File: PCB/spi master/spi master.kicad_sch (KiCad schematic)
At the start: 16 parts, among them J1 n8 Bus Connector, J2 Conn_01x09, U1 74LS08, U10 74HC273, U11 74HC245, U2 74LS393, U3 74HC04, U4 74LS139, U5 74HC595, U6 74HC165, U8 74HC74, U9 74LS153

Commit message: Worked on Spi master a little bit
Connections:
- net DIV0 is gone; now on net DEN: U10.2 (Q0), U11.2 (A0), U9.14 (S0)
- net DIV1 is gone; now on net DEN: U10.5 (Q1), U11.3 (A1), U9.2 (S1)
- net IEN is gone; now on net DEN: U1.13, U10.15 (Q5), U11.7 (A5)
- net ITC is gone; now on net DEN: U1.12, U11.9 (A7), U8.5 (Q)
- net SEL0 is gone; now on net DEN: U10.6 (Q2), U11.4 (A2), U4.2 (A0)
- net SEL1 is gone; now on net DEN: U10.9 (Q3), U11.5 (A3), U4.3 (A1)
- net UNUSED is gone; now on net DEN: U10.16 (Q6), U11.8 (A6)
- net ~{CS3} is gone; now on net ~{CS2}: J2.8 (Pin_8), U4.7 (O3)
- net CLK: now also U9.6 (I0a)
- net at U2.3 (Q0): no longer U9.6 (I0a)
- no-connect marks 20 -> 21
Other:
- note added: "Options: 1. CPU Clk 2. / 4 3. / 8 4. / 16 SPI clk is further divided by 2 so you get: 1. / 2 2. / 8 3. / 16 4. / 32 Slowest given cpu clock of 8mhz is 250khz and fastest is 4mhz"
- moved on the sheet: J1, J2, J?, R1, U10, U11, U1A, U1C, U1D, U1E, U2B, U2C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

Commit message: Working simulation...
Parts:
- removed unit 3 of U1
- removed unit 1 of U1
- removed unit 1 of U3
- removed unit 2 of U3
- removed U?: 74HC04, symbol 74xx:74HC04
- added U1: 74LS393, Package_DIP:DIP-14_W7.62mm, symbol 74xx:74LS393
- added U2: 74HC00, Package_DIP:DIP-14_W7.62mm, symbol 74xx:74HC00
- added unit 6 of U4
- added unit 1 of U4
- added unit 2 of U4
- added unit 5 of U4
- added unit 3 of U5
- added unit 2 of U5
- added unit 1 of U5
- J1: renamed from J2; footprint Connector_PinHeader_2.54mm:PinHeader_1x09_P2.54mm_Horizontal -> Connector_PinSocket_2.54mm:PinSocket_1x09_P2.54mm_Horizontal
- gave numbers to parts that had none: 2
- renumbered J1 to J2, U9 to U10, U10 to U11, U11 to U12, U4 to U3, U3 to U4, U1 to U5, U5 to U6, U6 to U7, U2 to U8, U8 to U9
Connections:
- net +5V: now also U1.7 (GND)
- net CLK: now also U5.13, U2.9
- net DEN: no longer U10.14 (S0), U10.2 (S1), U11.15 (Q5), U11.16 (Q6), U11.2 (Q0), U11.5 (Q1), U11.6 (Q2), U11.9 (Q3), U12.2 (A0), U12.3 (A1), U12.4 (A2), U12.5 (A3), U12.7 (A5), U12.8 (A6), U12.9 (A7), U3.2 (A0), U3.3 (A1), U5.12, U5.13, U9.5 (Q)
- net GND: now also U7.15 (~{CE}), U8.12 (MR)
- net MOSI: now also U2.6; no longer U7.10 (DS), U7.9 (Q7)
- net RUNNING: now also U2.2, U2.5
- net SPI_CLK: now also U1.3 (Q0), U4.13; no longer U7.2 (CP), U8.13 (CP)
- net TX_COMPLETE: now also U1.11 (Q0), U4.3; no longer U8.12 (MR)
- net ~{CR_WR}: now also U4.9; no longer U11.11 (Cp)
- net ~{DATA_RD}: now also U5.2
- net ~{DATA_WR}: now also U4.11, U5.1; no longer U7.1 (~{PL})
- net ~{IRQ}: now also U2.11; no longer U4.8
- net ~{RES}: now also U2.1, U5.10, U5.5; no longer U9.1 (~{R})
- net ~{TX_COMPLETE}: no longer U9.13 (~{R})
- net ~{CR_WR}_{QUAL}: now reaches U5.11
- net ~{CR_WR}_{QUAL}: now also U11.11 (Cp); no longer U4.9
- new net: U4.1, U7.9 (Q7)
- new net: U4.8, U5.12
- new net: U1.12 (MR), U1.2 (MR), U2.3
- new net: U1.13 (CP), U1.6 (Q3)
- new net: U2.4, U4.2
- new net: U2.10, U4.10
- new net: U4.4, U5.9
- new net: U5.3, U5.4
- new net DIV0: U10.14 (S0), U11.2 (Q0), U12.2 (A0)
- new net DIV1: U10.2 (S1), U11.5 (Q1), U12.3 (A1)
- new net IEN: U11.15 (Q5), U12.7 (A5), U2.13
- new net ITC: U12.9 (A7), U2.12, U9.5 (Q)
- new net SEL0: U11.6 (Q2), U12.4 (A2), U3.2 (A0)
- new net SEL1: U11.9 (Q3), U12.5 (A3), U3.3 (A1)
- new net UNUSED: U11.16 (Q6), U12.8 (A6)
- new net VCC: U7.10 (DS), U8.13 (CP)
- new net ~{DATA_WR}_{QUAL}: U2.8, U7.1 (~{PL})
- new net ~{DIV_CLK}: U1.1 (CP)
- new net ~{ITC_RES}: U5.6, U9.1 (~{R})
- new net ~{SPI_CLK}: U4.12, U7.2 (CP)
- new net ~{TX_COMPLETE_RES}: U5.8, U9.13 (~{R})
- no-connect marks 21 -> 27
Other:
- note added: "16 States 0: Idle 1-15: shifting 16: Transfer Complete"
- note added: "Does this need to be qualified with CLK?"
- note added: "Other Signal Generation"
- note removed: "CP pulses on HIGH to LOW transition. Do wee need to invert SPI_CLK here?"
- note removed: "Clock and Interrupt Generation"
- note removed: "Dividing by 16 because we want 8 full SPI_CLK cycles while ~{TX_COMPLETE} is HIGH"
- note removed: "Does this need to be qualified with CLK? Should CLK be inverted to meet the positive-edge trigger requirement for CR?"
- note removed: "TODO: may have to combine this with a “transfer started” clear flag"
- moved on the sheet: U4D, U5D, U8B

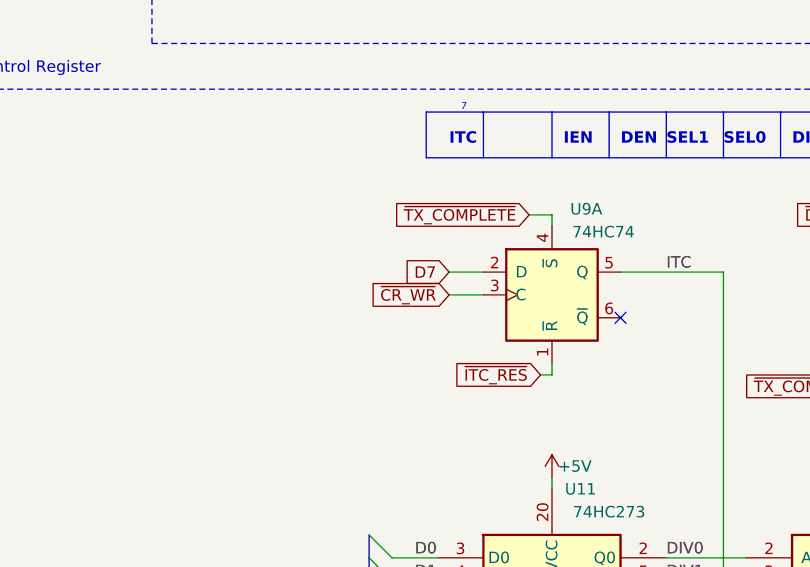
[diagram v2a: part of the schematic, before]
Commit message: circuit in Digital is working, tested in real world
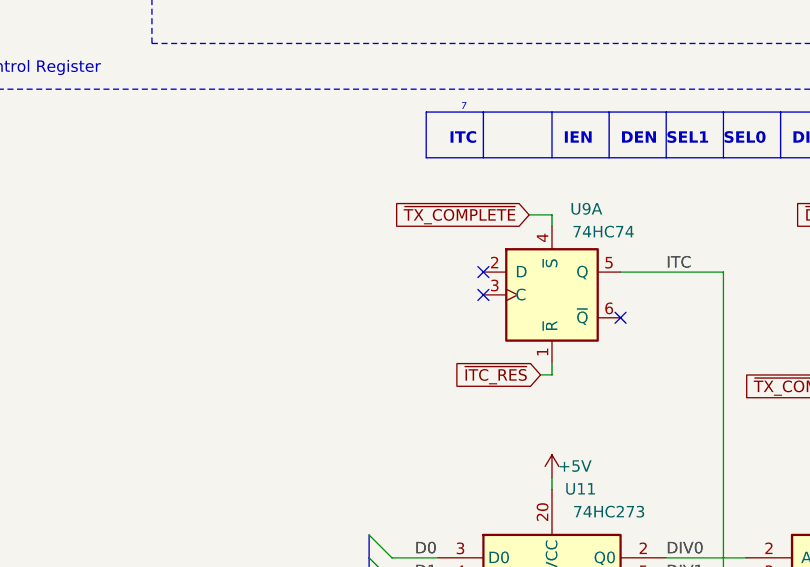
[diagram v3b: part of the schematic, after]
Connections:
- net D7: no longer U9.2 (D)
- net ~{CR_WR}: no longer U9.3 (C)
- no-connect marks 27 -> 29
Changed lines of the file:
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@@
 	)
 	(no_connect
+		(at 63.5 204.47)
+	)
+	(no_connect
 		(at 195.58 151.13)
 	)
@@
 	)
 	(no_connect
+		(at 63.5 207.01)
+	)
+	(no_connect
 		(at 303.53 200.66)
 	)
@@
 	(wire
 		(pts
-			(xy 59.69 204.47) (xy 63.5 204.47)
-		)
-		(stroke
-			(width 0)
-			(type default)
-		)
-	)
-	(wire
-		(pts
 			(xy 184.15 52.07) (xy 185.42 52.07)
 		)
@@
 		)
 	)
-	(wire
-		(pts
-			(xy 59.69 207.01) (xy 63.5 207.01)
-		)
-		(stroke
-			(width 0)
-			(type default)
-		)
-	)
 	(polyline
 		(pts
@@
 		)
 	)
-	(global_label "D7"
-		(shape input)
-		(at 59.69 204.47 180)
-		(fields_autoplaced yes)
-		(effects
-			(font
-				(size 1.27 1.27)
-			)
-			(justify right)
-		)
-		(property "Intersheetrefs" "${INTERSHEET_REFS}"
-			(at 54.8795 204.47 0)
-			(effects
-				(font
-					(size 1.27 1.27)
-				)
-				(justify right)
-				(hide yes)
-			)
-		)
-	)
 	(global_label "~{DATA_WR}"
 		(shape output)
@@
 			(effects
 				(font
-					(size 1.27 1.27)
-				)
-				(justify right)
-				(hide yes)
-			)
-		)
-	)
-	(global_label "~{CR_WR}"
-		(shape input)
-		(at 59.69 207.01 180)
-		(fields_autoplaced yes)
-		(effects
-			(font
-				(size 1.27 1.27)
-			)
-			(justify right)
-		)
-		(property "Intersheetrefs" "${INTERSHEET_REFS}"
-			(at 51.1368 206.9306 0)
-			(effects
-				(font

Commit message: 3 signals away from SPI Master PCB
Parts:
- removed J3, J4: Conn_01x06, symbol Connector_Generic:Conn_01x06
- removed R1: 20K, Resistor_THT:R_Axial_DIN0207_L6.3mm_D2.5mm_P5.08mm_Vertical, symbol Device:R_Small
- added C1, C10, C11, C12, C2, C3, C4, C5, C6, C7, C8, C9: 100nf, Capacitor_THT:C_Disc_D5.0mm_W2.5mm_P2.50mm, symbol Device:C_Small
- added C13: 220uf, Capacitor_THT:CP_Radial_D6.3mm_P2.50mm, symbol Device:C_Polarized_Small
- added J5: SD_CARD_PORT, Connector_PinSocket_2.54mm:PinSocket_2x08_P2.54mm_Vertical, symbol Connector_Generic:Conn_02x08_Odd_Even
- U1, U2, U4, U5, U8, U9: footprint Package_DIP:DIP-14_W7.62mm -> Package_DIP:DIP-14_W7.62mm_Socket
- U10, U6, U7: footprint Package_DIP:DIP-16_W7.62mm -> Package_DIP:DIP-16_W7.62mm_Socket
- U11, U12: footprint Package_DIP:DIP-20_W7.62mm -> Package_DIP:DIP-20_W7.62mm_Socket
- U4: footprint Package_DIP:DIP-14_W7.62mm -> (none)
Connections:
- net ~{DIV_CLK} is gone; now on net DIV_CLK: U1.1 (CP)
- net ~{TX_COMPLETE} is gone; now on net ~{TX_COMPLETE_RES}: U9.4 (~{S})
- net +5V: now also U1.14 (VCC), U2.14 (VCC), U5.12, U5.13, U6.10 (~{SRCLR}), U7.10 (DS), U8.1 (CP), U9.11 (C), U9.12 (D), U9.2 (D), U9.3 (C), C1.1, C10.1, C11.1, C12.1, C13.1, C2.1, C3.1, C4.1, C5.1, C6.1, C7.1, C8.1, C9.1, J5.11 (Pin_11), J5.12 (Pin_12); no longer U1.7 (GND)
- net A0: now also U3.13 (A1); no longer U3.14 (A0)
- net CLK: now also U8.13 (CP); no longer U5.13, U8.1 (CP)
- net GND: now also U1.7 (GND), U2.7 (GND), U4.1, C1.2, C10.2, C11.2, C12.2, C13.2, C2.2, C3.2, C4.2, C5.2, C6.2, C7.2, C8.2, C9.2, J5.1 (Pin_1), J5.15 (Pin_15), J5.16 (Pin_16), J5.2 (Pin_2)
- net MISO: now also J5.3 (Pin_3), J5.4 (Pin_4)
- net MOSI: now also J5.7 (Pin_7), J5.8 (Pin_8)
- net RUNNING: now also U12.8 (A6)
- net R~{W}: now also U3.14 (A0); no longer U3.13 (A1)
- net SPI_CLK: now also J5.5 (Pin_5), J5.6 (Pin_6)
- net ~{CS0}: now also J5.10 (Pin_10), J5.9 (Pin_9)
- net ~{CS2}: no longer J1.8 (Pin_8), U3.7 (O3)
- net ~{CS}: now also U4.11; no longer U3.15 (E)
- net ~{DATA_WR}: now also U7.1 (~{PL}); no longer U4.11
- net ~{RES}: no longer U6.10 (~{SRCLR})
- net at U7.9 (Q7): now also U4.9; no longer U4.1
- net at U4.8: now also U2.4; no longer U5.12
- net at U8.4 (Q1): no longer U10.5 (I1a)
- net at U8.5 (Q2): no longer U10.4 (I2a)
- net at U8.6 (Q3): no longer U10.3 (I3a)
- net at U8.10 (Q1): now also U10.5 (I1a)
- net at U8.8 (Q3): now also U10.3 (I3a)
- net at U8.9 (Q2): now also U10.4 (I2a)
- net at U4.2: no longer U2.4
- net UNUSED: no longer names the net of U11.16 (Q6)
- net UNUSED: no longer U12.8 (A6)
- removed net VCC: U7.10 (DS), U8.13 (CP)
- net ~{CR_RD} renamed ~{CTRL_RD}
- net ~{CR_WR} renamed ~{CTRL_WR}
- net ~{CTRL_WR}: now also U11.11 (Cp); no longer U4.9
- net ~{CR_WR}_{QUAL}: no longer names the net of U5.11
- net ~{CR_WR}_{QUAL}: no longer U11.11 (Cp)
- net ~{DATA_WR}_{QUAL} renamed ~{CS}_{QUAL}
- net ~{CS}_{QUAL}: now also U3.15 (E); no longer U7.1 (~{PL})
- new net ~{CS3}: J1.8 (Pin_8), U3.7 (O3)
- no-connect marks 29 -> 31
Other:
- note added: "BUSY"
- note removed: "Does this need to be qualified with CLK?"
- moved on the sheet: J1, U1C, U2C, U2D, U2E, U3C, U4A, U4B, U4E, U4F, U4G, U5A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

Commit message: rc1 for SPI Gate (prev SPI master) rc1 for Bouncer
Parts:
- added D1: LED, LED_SMD:LED_0805_2012Metric_Pad1.15x1.40mm_HandSolder, symbol Device:LED
- added R1: 330R, Resistor_SMD:R_0805_2012Metric_Pad1.20x1.40mm_HandSolder, symbol Device:R_Small
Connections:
- net +5V: now also R1.1
- net at U9.8 (~{Q}): now also D1.1 (K)
- new net: D1.2 (A), R1.2
- no-connect marks 31 -> 30
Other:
- note removed: "Does CLK need to be inverted to make this pos-edge triggered?"
- moved on the sheet: U11, U12, U3B, U9A, U9B
